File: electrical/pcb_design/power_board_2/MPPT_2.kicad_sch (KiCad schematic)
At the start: 14 parts

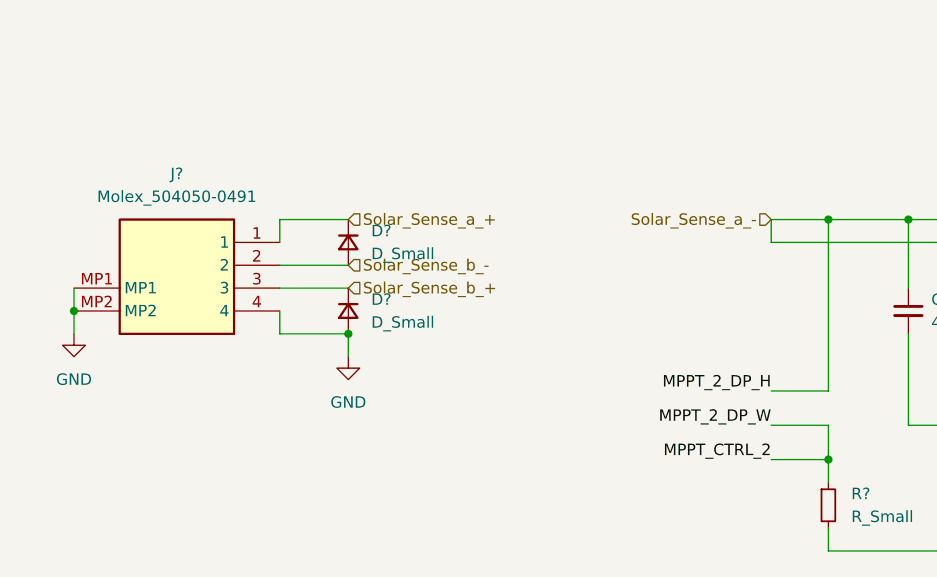
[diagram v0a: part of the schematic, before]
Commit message: mppt and solar sense schematic
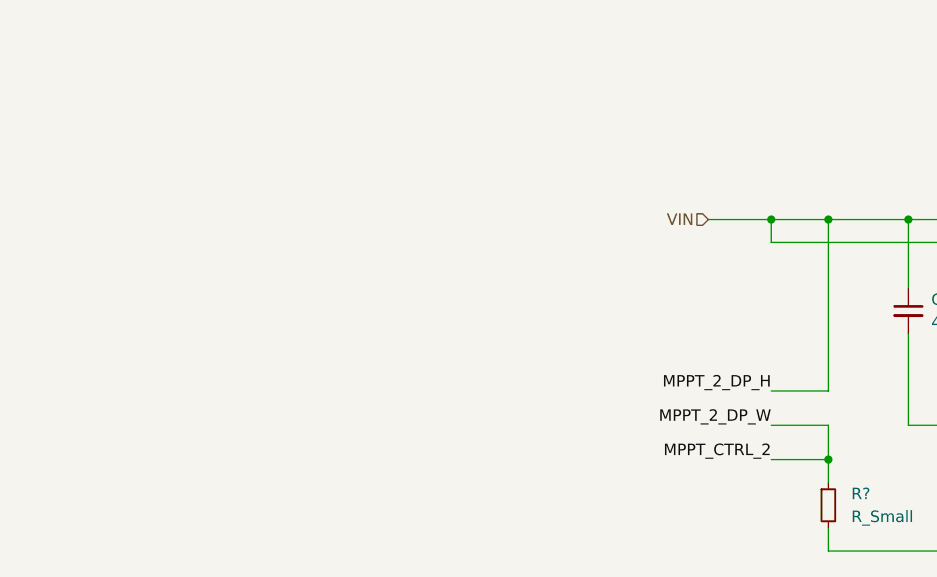
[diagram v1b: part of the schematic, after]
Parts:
- removed D? (x2): D_Small, symbol Device:D_Small
- removed J?: Molex_504050-0491, footprints:Molex_504050-0491, symbol tvsc_symbols:Molex_504050-0491
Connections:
- net Solar_Sense_a_- is gone; now on net VIN: C?.1, C?.1, U?. (WB), U?.2 (PVIN), U?.3 (VIN), U?.4 (RUN)
- net VIN: now reaches U?. (WB)

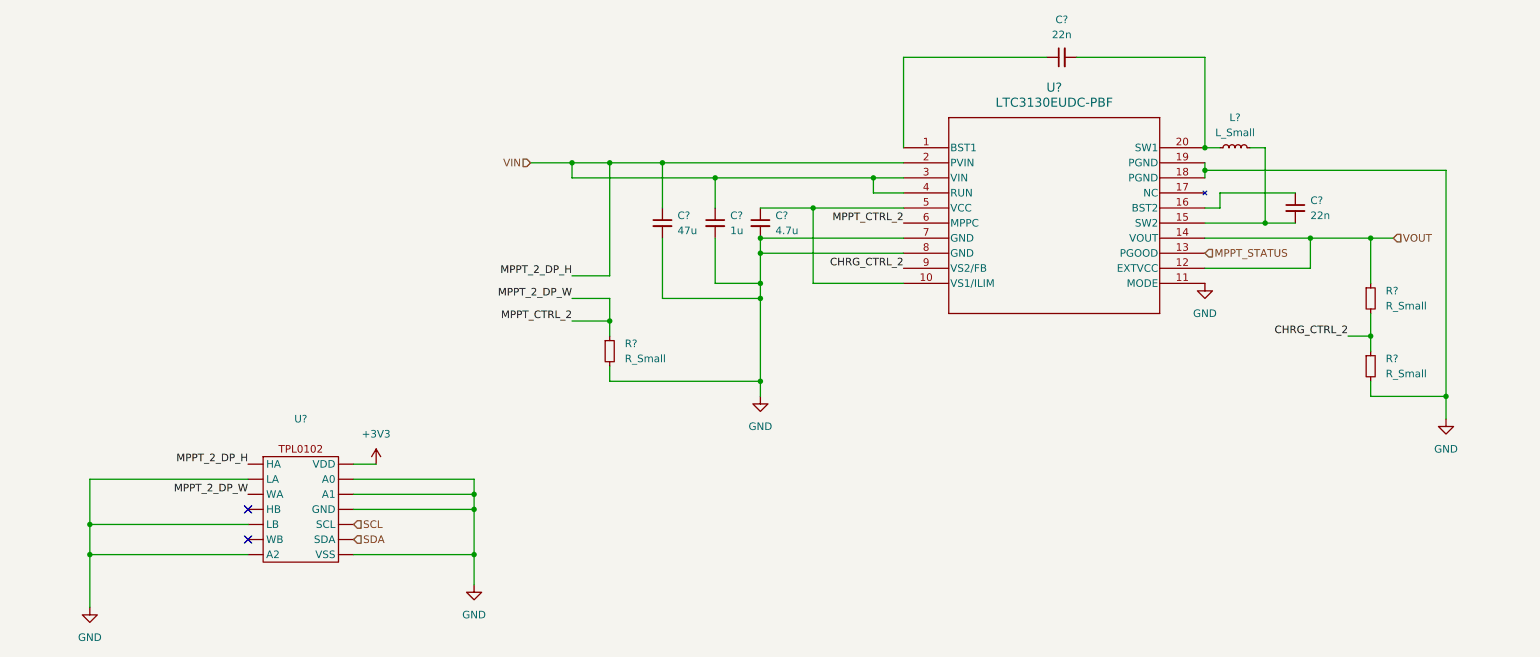
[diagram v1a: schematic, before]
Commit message: power board schematic complete except board id
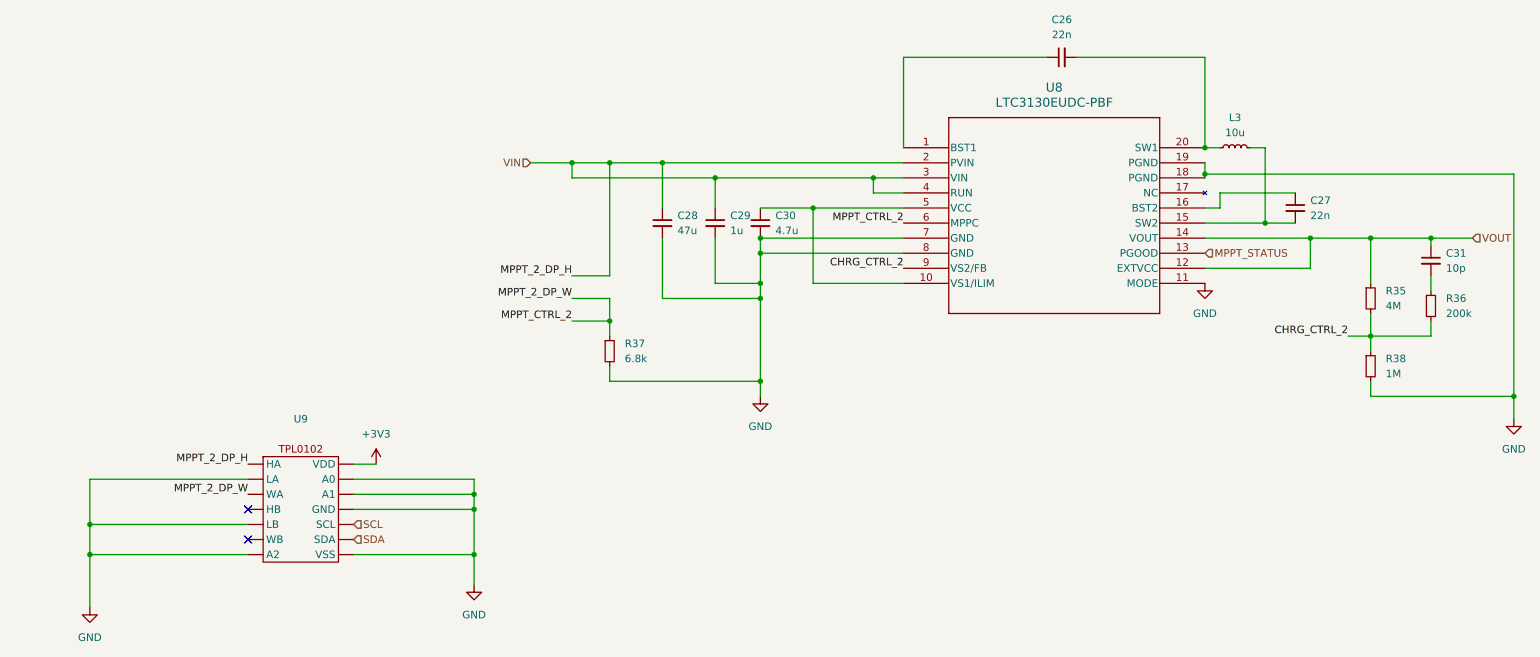
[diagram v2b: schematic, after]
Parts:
- added C31: 10p, symbol Device:C_Small
- added R36: 200k, symbol Device:R_Small
- L3: renamed from L?; value L_Small -> 10u
- R35: renamed from R?; value R_Small -> 4M
- R37: renamed from R?; value R_Small -> 6.8k
- R38: renamed from R?; value R_Small -> 1M
- gave numbers to parts that had none: 7
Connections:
- net CHRG_CTRL_2: now also R36.2
- net VOUT: now also C31.1
- new net: C31.2, R36.1

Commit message: smart bypass diode, schematic review edits
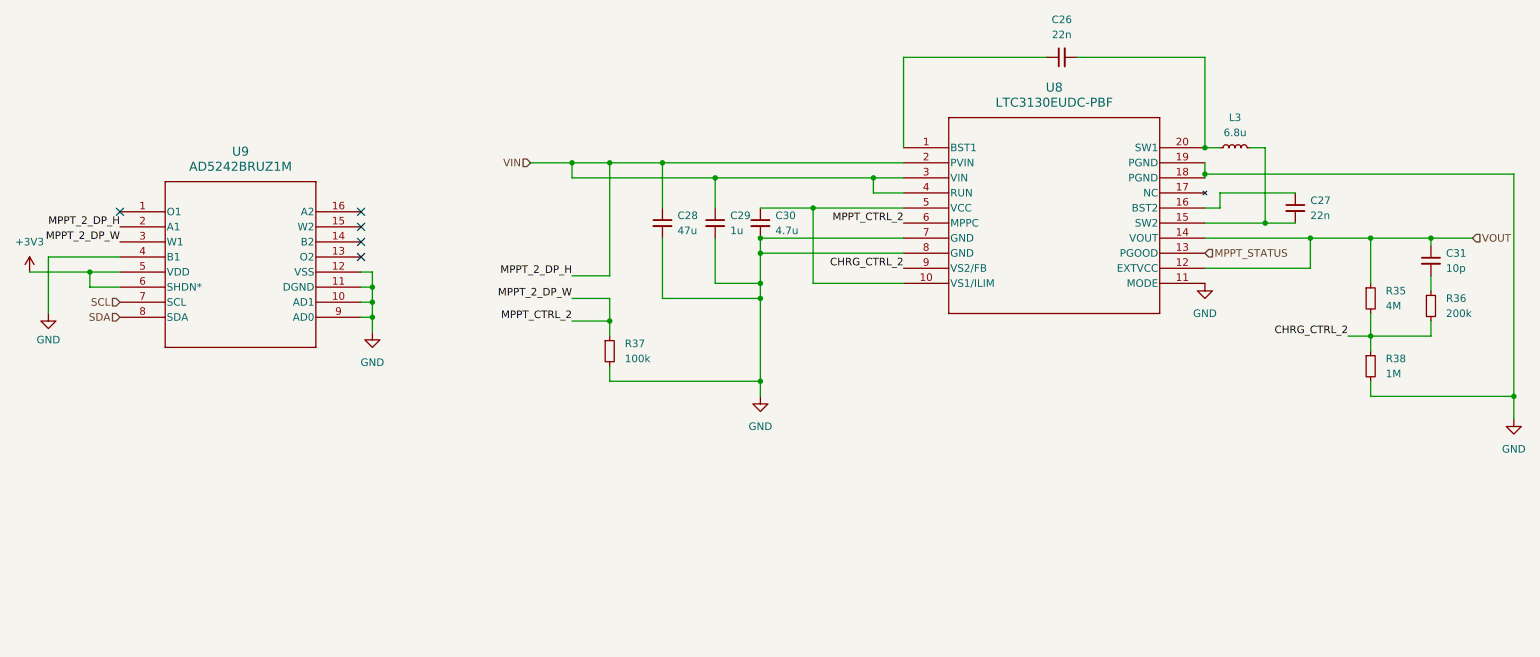
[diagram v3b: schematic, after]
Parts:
- removed U9: ~, symbol power_board_symbols:TPL0102
- added U9: AD5242BRUZ1M, RU_16_ADI, symbol TVSC:AD5242BRUZ1M
- L3: value 10u -> 6.8u
- R37: value 6.8k -> 100k
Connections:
- net +3V3: now also U9.5 (VDD), U9.6 (SHDN*)
- net GND: now also U9.10 (AD1), U9.11 (DGND), U9.12 (VSS), U9.4 (B1), U9.9 (AD0)
- net MPPT_2_DP_W: now also U9.3 (W1)
- net SCL: now also U9.7 (SCL)
- net SDA: now also U9.8 (SDA)
- net VIN: now also U9.2 (A1)
- no-connect marks 2 -> 5

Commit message: begin footprint assignment
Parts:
- U8: footprint UDC_20_ADI -> (none)
- U9: footprint RU_16_ADI -> (none)
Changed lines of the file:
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@@
 			)
 		)
-		(property "Footprint" "RU_16_ADI"
+		(property "Footprint" ""
 			(at 45.72 71.755 0)
 			(effects
@@
 			)
 		)
-		(property "Footprint" "UDC_20_ADI"
+		(property "Footprint" ""
 			(at 177.8 60.96 0)
 			(effects

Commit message: capacitor foot prints, need to learn how to stash
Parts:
- C26, C27, C28, C29, C30, C31: footprint (none) -> footprints:Nondescript_C_0402_1005Metric
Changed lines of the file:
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@@
 			)
 		)
-		(property "Footprint" ""
+		(property "Footprint" "footprints:Nondescript_C_0402_1005Metric"
 			(at 153.67 73.66 0)
 			(effects
@@
 			)
 		)
-		(property "Footprint" ""
+		(property "Footprint" "footprints:Nondescript_C_0402_1005Metric"
 			(at 243.84 71.12 0)
 			(effects
@@
 			)
 		)
-		(property "Footprint" ""
+		(property "Footprint" "footprints:Nondescript_C_0402_1005Metric"
 			(at 146.05 73.66 0)
 			(effects
@@
 			)
 		)
-		(property "Footprint" ""
+		(property "Footprint" "footprints:Nondescript_C_0402_1005Metric"
 			(at 204.47 45.72 0)
 			(effects
@@
 			)
 		)
-		(property "Footprint" ""
+		(property "Footprint" "footprints:Nondescript_C_0402_1005Metric"
 			(at 266.7 80.01 0)
 			(effects
@@
 			)
 		)
-		(property "Footprint" ""
+		(property "Footprint" "footprints:Nondescript_C_0402_1005Metric"
 			(at 137.16 73.66 0)
 			(effects

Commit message: footprint selection
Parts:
- U8: footprint (none) -> footprints:LTC3130
- U9: footprint (none) -> footprints:AD5242
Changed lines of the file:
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@@
 			)
 		)
-		(property "Footprint" ""
+		(property "Footprint" "footprints:AD5242"
 			(at 45.72 71.755 0)
 			(effects
@@
 			)
 		)
-		(property "Footprint" ""
+		(property "Footprint" "footprints:LTC3130"
 			(at 177.8 60.96 0)
 			(effects

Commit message: reristor selection
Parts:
- R35, R36, R37, R38: footprint (none) -> footprints:Nondescript_R_0402_1005Metric
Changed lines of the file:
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@@
 			)
 		)
-		(property "Footprint" ""
+		(property "Footprint" "footprints:Nondescript_R_0402_1005Metric"
 			(at 266.7 87.63 0)
 			(effects
@@
 			)
 		)
-		(property "Footprint" ""
+		(property "Footprint" "footprints:Nondescript_R_0402_1005Metric"
 			(at 256.54 97.79 0)
 			(effects
@@
 			)
 		)
-		(property "Footprint" ""
+		(property "Footprint" "footprints:Nondescript_R_0402_1005Metric"
 			(at 128.27 95.25 0)
 			(effects
@@
 			)
 		)
-		(property "Footprint" ""
+		(property "Footprint" "footprints:Nondescript_R_0402_1005Metric"
 			(at 256.54 86.36 0)
 			(effects
